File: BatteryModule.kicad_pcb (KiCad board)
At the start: 2 copper layers, 25 x 50 mm, 39 parts, among them J1 USB, J2 OUT, J3 USB_C_Receptacle_PowerOnly_6P, J4 BAT, U1 TLV76701DRVx, U2 TP4056-42-ESOP8, U3 TLV61048DBVR

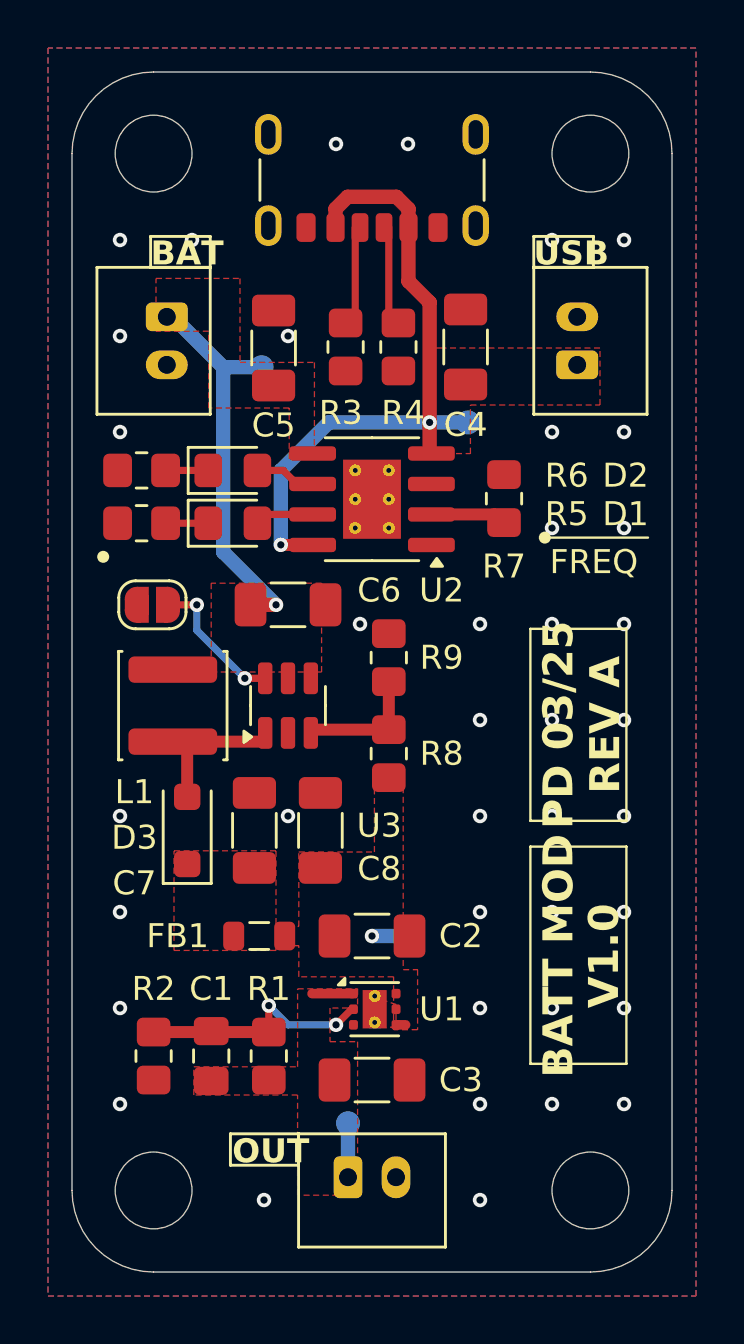
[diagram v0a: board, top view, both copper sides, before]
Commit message: Modified design structure
Added a battery sheet for the schematic.
Added a regulator sheet for the schematic.
Updated board layout.
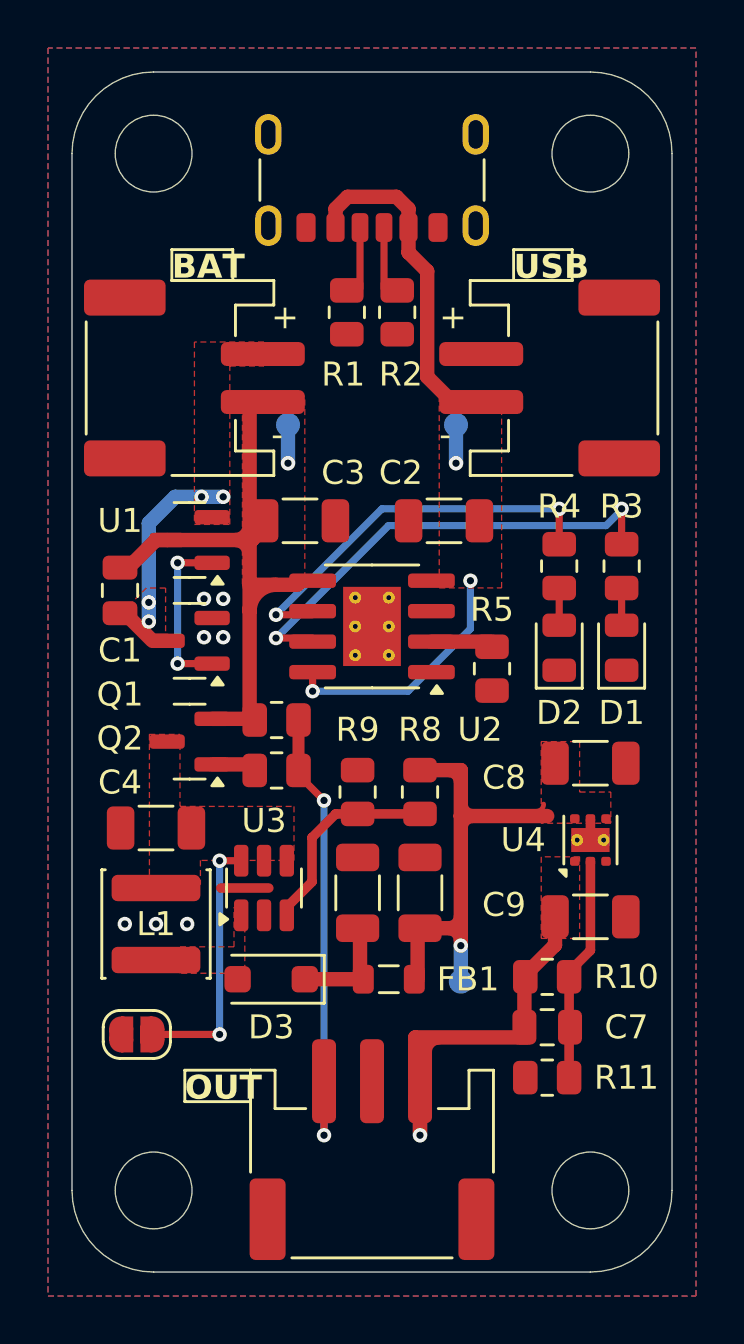
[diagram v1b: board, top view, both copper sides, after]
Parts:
- added C9: 2u2, Capacitor_SMD:C_1206_3216Metric, F.Cu at (151.6, 115.2)
- added Q1: SI2312BDS, Package_TO_SOT_SMD:SOT-23, F.Cu at (134.9, 103.7)
- added Q2: SI2301BDS, Package_TO_SOT_SMD:SOT-23, F.Cu at (134.9, 107.9)
- added R10: 10K, Resistor_SMD:R_0805_2012Metric, F.Cu at (149.8, 117.7)
- added R11: 102K, Resistor_SMD:R_0805_2012Metric, F.Cu at (149.8, 121.9)
- added U4: TLV76701DRVx, Package_SON:WSON-6-1EP_2x2mm_P0.65mm_EP1x1.6mm_ThermalVias, F.Cu at (151.6, 112.0)
- C1: value 10p -> 100n; footprint Capacitor_SMD:C_0805_2012Metric_Pad1.18x1.45mm_HandSolder -> Capacitor_SMD:C_0805_2012Metric
- C2, C3: value 2u2 -> 10u; footprint Capacitor_SMD:C_1206_3216Metric_Pad1.33x1.80mm_HandSolder -> Capacitor_SMD:C_1206_3216Metric
- C4, C5: value 10u -> 2u2; footprint Capacitor_SMD:C_1206_3216Metric_Pad1.33x1.80mm_HandSolder -> Capacitor_SMD:C_1206_3216Metric
- C6, C8: footprint Capacitor_SMD:C_1206_3216Metric_Pad1.33x1.80mm_HandSolder -> Capacitor_SMD:C_1206_3216Metric
- C7: value 2u2 -> 10p; footprint Capacitor_SMD:C_1206_3216Metric_Pad1.33x1.80mm_HandSolder -> Capacitor_SMD:C_0805_2012Metric
- D1, D2: footprint LED_SMD:LED_0805_2012Metric_Pad1.15x1.40mm_HandSolder -> LED_SMD:LED_0805_2012Metric
- J1: footprint Custom_Parts:JST_PH_1x02_P2.00MM_VERT -> Custom_Parts:JST_PH_1x02_P2.00MM_SMD_HOR
- J2: value OUT -> USB_C_Receptacle_PowerOnly_6P; footprint Custom_Parts:JST_PH_1x02_P2.00MM_VERT -> Connector_USB:USB_C_Receptacle_GCT_USB4125-xx-x_6P_TopMnt_Horizontal
- J3: value USB_C_Receptacle_PowerOnly_6P -> BAT; footprint Connector_USB:USB_C_Receptacle_GCT_USB4125-xx-x_6P_TopMnt_Horizontal -> Custom_Parts:JST_PH_1x02_P2.00MM_SMD_HOR
- J4: value BAT -> OUT; footprint Custom_Parts:JST_PH_1x02_P2.00MM_VERT -> Custom_Parts:JST_PH_1x03_P2.00MM_SMD_HOR
- R1: value 10K -> 5K1; footprint Resistor_SMD:R_0805_2012Metric_Pad1.20x1.40mm_HandSolder -> Resistor_SMD:R_0805_2012Metric
- R2: value 102K -> 5K1; footprint Resistor_SMD:R_0805_2012Metric_Pad1.20x1.40mm_HandSolder -> Resistor_SMD:R_0805_2012Metric
- R3, R4: value 5K1 -> 1K; footprint Resistor_SMD:R_0805_2012Metric_Pad1.20x1.40mm_HandSolder -> Resistor_SMD:R_0805_2012Metric
- R5: value 1K -> 2K2; footprint Resistor_SMD:R_0805_2012Metric_Pad1.20x1.40mm_HandSolder -> Resistor_SMD:R_0805_2012Metric
- R6: value 1K -> 1M; footprint Resistor_SMD:R_0805_2012Metric_Pad1.20x1.40mm_HandSolder -> Resistor_SMD:R_0805_2012Metric
- R7: value 2K2 -> 10K; footprint Resistor_SMD:R_0805_2012Metric_Pad1.20x1.40mm_HandSolder -> Resistor_SMD:R_0805_2012Metric
- R8, R9: footprint Resistor_SMD:R_0805_2012Metric_Pad1.20x1.40mm_HandSolder -> Resistor_SMD:R_0805_2012Metric
- TP1: value LDO -> USB
- TP2: value USB -> BAT
- TP3: value BAT -> BST
- TP4: value BST -> LDO
- U1: value TLV76701DRVx -> ME2801; footprint Package_SON:WSON-6-1EP_2x2mm_P0.65mm_EP1x1.6mm_ThermalVias -> Package_TO_SOT_SMD:SOT-23
- moved J2 42.7 mm to (142.5, 83.4), turned to 180 degrees
- moved J4 35.7 mm to (142.5, 124.9), turned to 0 degrees
- moved R2 32.6 mm to (143.6, 90.0)
- moved R1 31.2 mm to (141.5, 90.0)
- moved TP1 29.4 mm to (146.0, 94.7)
- moved TP3 26.9 mm to (146.2, 117.9)
- moved C4 23.8 mm to (133.5, 111.5), turned to 180 degrees
- moved C3 23.5 mm to (139.5, 98.7)
- moved C5 23.0 mm to (141.9, 114.2)
- moved U1 21.0 mm to (134.9, 99.5), turned to 180 degrees
- moved C1 19.8 mm to (132.0, 101.6)
- moved JP1 17.9 mm to (132.7, 120.1)
- moved C2 17.6 mm to (145.5, 98.7), turned to 180 degrees
- moved D1 17.0 mm to (152.9, 104.0), turned to 90 degrees
- moved R5 15.8 mm to (147.5, 104.9), turned to -90 degrees
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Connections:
- C1 pad 1: Net-(U1-FB) -> VBAT
- C1 pad 2: 9V -> GBAT
- C2 pad 1: 10V5 -> VUSB
- C3 pad 1: 9V -> VBAT
- C4 pad 1: VUSB -> VREG
- C5 pad 1: VBAT -> Net-(D3-K)
- C6 pad 1: VBAT -> 10V5
- C7 pad 1: Net-(D3-K) -> Net-(U4-FB)
- C7 pad 2: GND -> 9V
- D1 pad 1: Net-(D1-K) -> GND
- D2 pad 1: Net-(D2-K) -> GND
- J4 pad 1: VBAT -> BATSW
- L1 pad 1: VBAT -> VREG
- R1 pad 1: Net-(U1-FB) -> Net-(J2-CC2)
- R1 pad 2: 9V -> GND
- R2 pad 1: Net-(U1-FB) -> Net-(J2-CC1)
- R3 pad 1: Net-(J3-CC2) -> Net-(D1-A)
- R3 pad 2: GND -> Net-(U2-~{CHRG})
- R4 pad 1: Net-(J3-CC1) -> Net-(D2-A)
- R4 pad 2: GND -> Net-(U2-~{STDBY})
- R5 pad 1: Net-(D1-K) -> Net-(U2-PROG)
- R6 pad 1: Net-(D2-K) -> VBAT
- R6 pad 2: GND -> BATSW
- R7 pad 1: Net-(U2-PROG) -> Net-(Q2-G)
- R7 pad 2: GND -> BATSW
- TP1 pad 1: 9V -> VUSB
- TP2 pad 1: VUSB -> VBAT
- TP3 pad 1: VBAT -> 10V5
- TP4 pad 1: 10V5 -> 9V
- U1 pad 1: 9V -> Net-(Q1-G)
- U1 pad 2: Net-(U1-FB) -> GBAT
- U1 pad 3: GND -> VBAT
- U2 pad 6: Net-(D2-A) -> Net-(U2-~{STDBY})
- U2 pad 7: Net-(D1-A) -> Net-(U2-~{CHRG})
- U3 pad 4: VBAT -> VREG
- U3 pad 5: VBAT -> VREG
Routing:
- net BATSW: track 0.00 -> 19.8 mm, vias 0 -> 2
- net Net-(U2-~{CHRG}): track 0.00 -> 19.7 mm, vias 0 -> 2
- net Net-(U2-~{STDBY}): track 0.00 -> 16.6 mm, vias 0 -> 2
- net 10V5: track 2.00 -> 17.2 mm
- net 9V: track 3.95 -> 15.2 mm, vias 0 -> 1
- net Net-(U1-FB): track 10.0 -> 0.00 mm, vias 2 -> 0
- net GBAT: track 0.00 -> 9.74 mm, vias 0 -> 4
- net Net-(U4-FB): track 0.00 -> 9.33 mm
- net VBAT: track 16.7 -> 24.3 mm
- net Net-(Q1-G): track 0.00 -> 7.08 mm, vias 0 -> 2
- net Net-(D3-A): track 6.10 -> 0.00 mm
- net Net-(JP1-B): track 5.94 -> 10.9 mm
- net Net-(D3-K): track 0.00 -> 4.33 mm
- net Net-(J3-CC2): track 3.52 -> 0.00 mm
- net Net-(J3-CC1): track 3.52 -> 0.00 mm
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- added copper zone on F.Cu, net GBAT
- added copper zone on F.Cu, net Net-(D3-A)
- added copper zone on F.Cu, net VREG
- removed copper zone on F.Cu, net Net-(D3-K)
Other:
- board text added: "+"
- board text added: "-"
- board text removed: "BATT MOD"
- board text removed: "D1"
- board text removed: "D2"
- board text removed: "FREQ"
- board text removed: "PD 03/25"
- board text removed: "R5"
- board text removed: "R6"
- board text removed: "REV A"
- board text removed: "V1.0"

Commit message: Schematic and board layout
Updated the project schematic.
Updated the board layout.
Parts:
- added G***: LOGO, Logos:Cat, F.Cu at (146.1, 106.2)
- added R12: 10K, Resistor_SMD:R_0805_2012Metric, F.Cu at (146.9, 117.0)
- D1: value CHRG -> STBY
- D2: value FULL -> CHRG
- Q1, Q2, U1: footprint Package_TO_SOT_SMD:SOT-23 -> Custom_Parts:SOT-23_NO_MARK
- R1: value 5K1 -> 10K
- R2: value 5K1 -> 1K
- R4: value 1K -> 5K1
- R5: value 2K2 -> 5K1
- R6: value 1M -> 2K2
- R7: value 10K -> 1M
- moved R10 16.5 mm to (135.3, 109.8)
- moved R5 15.6 mm to (143.6, 89.8)
- moved R4 14.0 mm to (141.5, 89.8), turned to -90 degrees
- moved R2 13.8 mm to (152.7, 100.4)
- moved R1 13.6 mm to (132.2, 100.0)
- moved R6 11.1 mm to (147.4, 100.4), turned to 90 degrees
- moved C8 6.56 mm to (145.5, 111.2), turned to 90 degrees
- moved TP4 5.91 mm to (148.8, 118.7)
- moved R8 5.86 mm to (139.1, 107.7), turned to 0 degrees
- moved C6 5.75 mm to (139.1, 112.2), turned to 180 degrees
- moved R11 5.02 mm to (150.9, 117.0), turned to -90 degrees
- moved TP3 4.58 mm to (143.8, 114.0)
- moved C9 4.00 mm to (152.0, 111.2), turned to 90 degrees
- moved FB1 3.97 mm to (142.5, 113.9), turned to -90 degrees
- moved C2 3.96 mm to (143.8, 95.1), turned to 90 degrees
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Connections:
- D1 pad 1: GND -> Net-(D1-K)
- D1 pad 2: Net-(D1-A) -> VUSB
- D2 pad 1: GND -> Net-(D2-K)
- D2 pad 2: Net-(D2-A) -> VUSB
- Q1 pad 2: GND -> GBAT
- Q1 pad 3: GBAT -> GND
- R1 pad 1: Net-(J2-CC2) -> Net-(U1-SET)
- R1 pad 2: GND -> Net-(Q1-G)
- R10 pad 1: Net-(U4-FB) -> Net-(U3-FB)
- R10 pad 2: 9V -> GND
- R11 pad 2: GND -> 9V
- R2 pad 1: Net-(J2-CC1) -> Net-(U2-~{STDBY})
- R2 pad 2: GND -> Net-(D1-K)
- R3 pad 1: Net-(D1-A) -> Net-(U2-~{CHRG})
- R3 pad 2: Net-(U2-~{CHRG}) -> Net-(D2-K)
- R4 pad 1: Net-(D2-A) -> Net-(J2-CC2)
- R4 pad 2: Net-(U2-~{STDBY}) -> GND
- R5 pad 1: Net-(U2-PROG) -> Net-(J2-CC1)
- R6 pad 1: VBAT -> Net-(U2-PROG)
- R6 pad 2: BATSW -> GND
- R7 pad 1: Net-(Q2-G) -> VBAT
- R8 pad 1: Net-(U3-FB) -> Net-(Q2-G)
- R8 pad 2: 10V5 -> BATSW
- R9 pad 2: GND -> 10V5
- U1 pad 1: Net-(Q1-G) -> Net-(U1-SET)
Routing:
- net VBAT: track 24.3 -> 3.61 mm
- net VUSB: track 26.3 -> 43.9 mm, vias 3 -> 4
- net 10V5: track 17.2 -> 1.30 mm
- net 9V: track 15.2 -> 1.30 mm
- net Net-(U1-SET): track 0.00 -> 13.6 mm, vias 0 -> 2
- net Net-(U3-FB): track 8.03 -> 1.99 mm
- net GBAT: track 9.74 -> 4.04 mm
- net GND: track 2.85 -> 8.49 mm, vias 7 -> 47
- net Net-(D3-K): track 4.33 -> 0.00 mm
- net Net-(U2-~{STDBY}): track 16.6 -> 20.3 mm
- net Net-(Q1-G): track 7.08 -> 4.05 mm, vias 2 -> 0
- net Net-(JP1-B): track 10.9 -> 8.63 mm
- net Net-(D2-K): track 0.00 -> 1.55 mm
- net Net-(D2-A): track 1.55 -> 0.00 mm
- net Net-(D1-K): track 0.00 -> 1.55 mm
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- added copper zone on B.Cu, net GBAT
- added copper zone on F.Cu, net Net-(D3-K)
- added copper zone on F.Cu, net Net-(U3-FB)
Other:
- board text added: "CH"
- board text added: "PD 04/25"
- board text added: "SB"
- board text added: "V1.2 REV A"
